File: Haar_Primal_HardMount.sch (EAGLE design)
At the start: 10 parts, among them J1 SOLDERCUP_CONN_QUAD, Q1 DMG3404, U1 SHT30DFN, U4 DPS368

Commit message: Updated Hard Mount - Variable address jumper
Added jumper to Hard Mount to allow for a variable address configuration
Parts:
- removed H2: (no value), bschulz:MOUNTING_HOLE2_NP
- added JP2: JUMPER-SMT_2_NO_SILK, bschulz:JUMPER-SMT_2_NO_SILK
- added R3: 10k, bschulz_passives:R-EU_10KR0603
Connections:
- new net ADDR: JP2.1, R3.2, U1.ADDR, U4.CSB
- net 3V3: now also JP2.2; no longer U4.CSB
- net GND: now also R3.1; no longer U1.ADDR
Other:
- moved on the sheet: C1, U4
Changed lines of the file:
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@@
 <setting verticaltext="up"/>
 </settings>
-<grid distance="0.1" unitdist="inch" unit="inch" style="lines" multiple="1" display="no" altdistance="0.01" altunitdist="inch" altunit="inch"/>
+<grid distance="0.1" unitdist="inch" unit="mm" style="lines" multiple="1" display="no" altdistance="0.01" altunitdist="inch" altunit="inch"/>
 <layers>
 <layer number="1" name="Top" color="4" fill="1" visible="no" active="no"/>
@@
 <part name="U1" library="bschulz" deviceset="SHT3*" device="DFN" technology="0" value="SHT30DFN"/>
 <part name="GND3" library="supply1" library_urn="urn:adsk.eagle:library:371" deviceset="GND" device=""/>
-<part name="H2" library="bschulz" deviceset="MOUNTING_HOLE" device="2_NP"/>
 <part name="JP1" library="bschulz" deviceset="JUMPER-SMT_3_2-NC_TRACE" device="_SILK" package3d_urn="urn:adsk.eagle:package:39289/1"/>
+<part name="R3" library="bschulz_passives" deviceset="R-EU_" device="R0603" technology="10K" value="10k"/>
+<part name="GND1" library="supply1" library_urn="urn:adsk.eagle:library:371" deviceset="GND" device=""/>
+<part name="JP2" library="bschulz" deviceset="JUMPER-SMT_2_NO" device="_SILK" package3d_urn="urn:adsk.eagle:package:39279/1"/>
 </parts>
 <sheets>
@@
 <attribute name="VALUE" x="41.402" y="62.23" size="1.778" layer="96" rot="R90"/>
 </instance>
-<instance part="U4" gate="G$1" x="93.98" y="27.94" smashed="yes">
-<attribute name="DISP" x="92.71" y="37.084" size="1.778" layer="95" align="center"/>
-<attribute name="NAME" x="92.71" y="21.59" size="1.27" layer="95" ratio="15" align="center"/>
-</instance>
-<instance part="C1" gate="G$1" x="68.58" y="30.48" smashed="yes">
-<attribute name="NAME" x="70.104" y="30.861" size="1.778" layer="95"/>
-<attribute name="VALUE" x="70.104" y="25.781" size="1.778" layer="96"/>
-</instance>
-<instance part="GND2" gate="1" x="76.2" y="20.32" smashed="yes">
-<attribute name="VALUE" x="73.66" y="17.78" size="1.778" layer="96"/>
+<instance part="U4" gate="G$1" x="93.98" y="55.88" smashed="yes">
+<attribute name="DISP" x="92.71" y="65.024" size="1.778" layer="95" align="center"/>
+<attribute name="NAME" x="92.71" y="49.53" size="1.27" layer="95" ratio="15" align="center"/>
+</instance>
+<instance part="C1" gate="G$1" x="58.42" y="58.42" smashed="yes">
+<attribute name="NAME" x="59.944" y="58.801" size="1.778" layer="95"/>
+<attribute name="VALUE" x="59.944" y="53.721" size="1.778" layer="96"/>
+</instance>
+<instance part="GND2" gate="1" x="76.2" y="48.26" smashed="yes">
+<attribute name="VALUE" x="73.66" y="45.72" size="1.778" layer="96"/>
 </instance>
 <instance part="U1" gate="G$1" x="33.02" y="27.94" smashed="yes">
@@
 <attribute name="VALUE" x="12.7" y="15.24" size="1.778" layer="96"/>
 </instance>
-<instance part="H2" gate="G$1" x="78.74" y="86.36" smashed="yes">
-<attribute name="NAME" x="80.772" y="86.9442" size="1.778" layer="95"/>
-<attribute name="VALUE" x="80.772" y="83.8962" size="1.778" layer="96"/>
-</instance>
 <instance part="JP1" gate="G$1" x="33.02" y="73.66" smashed="yes" rot="R270">
 <attribute name="NAME" x="33.401" y="71.12" size="1.778" layer="95" font="vector" rot="R270"/>
+</instance>
+<instance part="R3" gate="G$1" x="76.2" y="12.7" smashed="yes" rot="R90">
+<attribute name="NAME" x="74.7014" y="8.89" size="1.778" layer="95" rot="R90"/>
+<attribute name="VALUE" x="79.502" y="8.89" size="1.778" layer="96" rot="R90"/>
+</instance>
+<instance part="GND1" gate="1" x="76.2" y="2.54" smashed="yes">
+<attribute name="VALUE" x="73.66" y="0" size="1.778" layer="96"/>
+</instance>
+<instance part="JP2" gate="G$1" x="76.2" y="25.4" smashed="yes" rot="R90">
+<attribute name="NAME" x="73.66" y="22.86" size="1.778" layer="95" font="vector" rot="R90"/>
 </instance>
 </instances>
@@
 <segment>
 <pinref part="U4" gate="G$1" pin="GND"/>
-<wire x1="78.74" y1="25.4" x2="76.2" y2="25.4" width="0.1524" layer="91"/>
-<wire x1="76.2" y1="25.4" x2="76.2" y2="22.86" width="0.1524" layer="91"/>
+<wire x1="78.74" y1="53.34" x2="76.2" y2="53.34" width="0.1524" layer="91"/>
+<wire x1="76.2" y1="53.34" x2="76.2" y2="50.8" width="0.1524" layer="91"/>
 <pinref part="GND2" gate="1" pin="GND"/>
 <pinref part="C1" gate="G$1" pin="2"/>
-<wire x1="68.58" y1="25.4" x2="76.2" y2="25.4" width="0.1524" layer="91"/>
-<junction x="76.2" y="25.4"/>
-</segment>
-<segment>
-<pinref part="U1" gate="G$1" pin="ADDR"/>
+<wire x1="58.42" y1="53.34" x2="76.2" y2="53.34" width="0.1524" layer="91"/>
+<junction x="76.2" y="53.34"/>
+</segment>
+<segment>
 <pinref part="U1" gate="G$1" pin="VSS"/>
-<wire x1="17.78" y1="27.94" x2="17.78" y2="22.86" width="0.1524" layer="91"/>
 <wire x1="17.78" y1="22.86" x2="15.24" y2="22.86" width="0.1524" layer="91"/>
-<junction x="17.78" y="22.86"/>
 <wire x1="15.24" y1="22.86" x2="15.24" y2="20.32" width="0.1524" layer="91"/>
 <pinref part="GND3" gate="1" pin="GND"/>
+</segment>
+<segment>
+<pinref part="GND1" gate="1" pin="GND"/>
+<pinref part="R3" gate="G$1" pin="1"/>
+<wire x1="76.2" y1="5.08" x2="76.2" y2="7.62" width="0.1524" layer="91"/>
 </segment>
 </net>
@@
 <pinref part="U4" gate="G$1" pin="VDD"/>
 <pinref part="U4" gate="G$1" pin="VDDIO"/>
-<wire x1="78.74" y1="30.48" x2="78.74" y2="33.02" width="0.1524" layer="91"/>
-<junction x="78.74" y="33.02"/>
+<wire x1="78.74" y1="58.42" x2="78.74" y2="60.96" width="0.1524" layer="91"/>
+<junction x="78.74" y="60.96"/>
 <pinref part="C1" gate="G$1" pin="1"/>
-<wire x1="78.74" y1="33.02" x2="68.58" y2="33.02" width="0.1524" layer="91"/>
-<wire x1="68.58" y1="33.02" x2="63.5" y2="33.02" width="0.1524" layer="91"/>
-<junction x="68.58" y="33.02"/>
-<label x="63.5" y="33.02" size="0.8128" layer="95" rot="R180" xref="yes"/>
-<pinref part="U4" gate="G$1" pin="CSB"/>
-<wire x1="78.74" y1="30.48" x2="78.74" y2="27.94" width="0.1524" layer="91"/>
-<junction x="78.74" y="30.48"/>
+<wire x1="78.74" y1="60.96" x2="58.42" y2="60.96" width="0.1524" layer="91"/>
+<wire x1="58.42" y1="60.96" x2="53.34" y2="60.96" width="0.1524" layer="91"/>
+<junction x="58.42" y="60.96"/>
+<label x="53.34" y="60.96" size="0.8128" layer="95" rot="R180" xref="yes"/>
 </segment>
 <segment>
@@
 <label x="142.24" y="27.94" size="1.778" layer="95" rot="R180" xref="yes"/>
 </segment>
+<segment>
+<pinref part="JP2" gate="G$1" pin="2"/>
+<wire x1="76.2" y1="30.48" x2="76.2" y2="33.02" width="0.1524" layer="91"/>
+<wire x1="76.2" y1="33.02" x2="78.74" y2="33.02" width="0.1524" layer="91"/>
+<label x="78.74" y="33.02" size="1.27" layer="95" xref="yes"/>
+</segment>
 </net>
 <net name="SDA" class="0">
@@
 <segment>
 <pinref part="U4" gate="G$1" pin="SDI"/>
-<wire x1="106.68" y1="33.02" x2="114.3" y2="33.02" width="0.1524" layer="91"/>
-<label x="106.68" y="33.02" size="1.27" layer="95"/>
+<wire x1="106.68" y1="60.96" x2="114.3" y2="60.96" width="0.1524" layer="91"/>
+<label x="106.68" y="60.96" size="1.27" layer="95"/>
 </segment>
 <segment>
@@
 <segment>
 <pinref part="U4" gate="G$1" pin="SCK"/>
-<wire x1="106.68" y1="30.48" x2="114.3" y2="30.48" width="0.1524" layer="91"/>
-<label x="106.68" y="30.48" size="1.27" layer="95"/>
+<wire x1="106.68" y1="58.42" x2="114.3" y2="58.42" width="0.1524" layer="91"/>
+<label x="106.68" y="58.42" size="1.27" layer="95"/>
 </segment>
 <segment>
@@
 <segment>
 <pinref part="U4" gate="G$1" pin="SDO"/>
-<wire x1="106.68" y1="27.94" x2="114.3" y2="27.94" width="0.1524" layer="91"/>
-<label x="106.68" y="27.94" size="1.778" layer="95"/>
+<wire x1="106.68" y1="55.88" x2="114.3" y2="55.88" width="0.1524" layer="91"/>
+<label x="106.68" y="55.88" size="1.778" layer="95"/>
 </segment>
 </net>
@@
 </segment>
 </net>
+<net name="ADDR" class="0">
+<segment>
+<pinref part="U1" gate="G$1" pin="ADDR"/>
+<wire x1="17.78" y1="27.94" x2="15.24" y2="27.94" width="0.1524" layer="91"/>
+<label x="15.24" y="27.94" size="1.27" layer="95" rot="R180" xref="yes"/>
+</segment>
+<segment>
+<pinref part="U4" gate="G$1" pin="CSB"/>
+<wire x1="78.74" y1="55.88" x2="76.2" y2="55.88" width="0.1524" layer="91"/>
+<label x="76.2" y="55.88" size="1.27" layer="95" rot="R180" xref="yes"/>
+</segment>
+<segment>
+<pinref part="R3" gate="G$1" pin="2"/>
+<wire x1="76.2" y1="17.78" x2="76.2" y2="20.32" width="0.1524" layer="91"/>
+<wire x1="76.2" y1="20.32" x2="78.74" y2="20.32" width="0.1524" layer="91"/>
+<label x="78.74" y="20.32" size="1.27" layer="95" xref="yes"/>
+<pinref part="JP2" gate="G$1" pin="1"/>
+<junction x="76.2" y="20.32"/>
+</segment>
+</net>

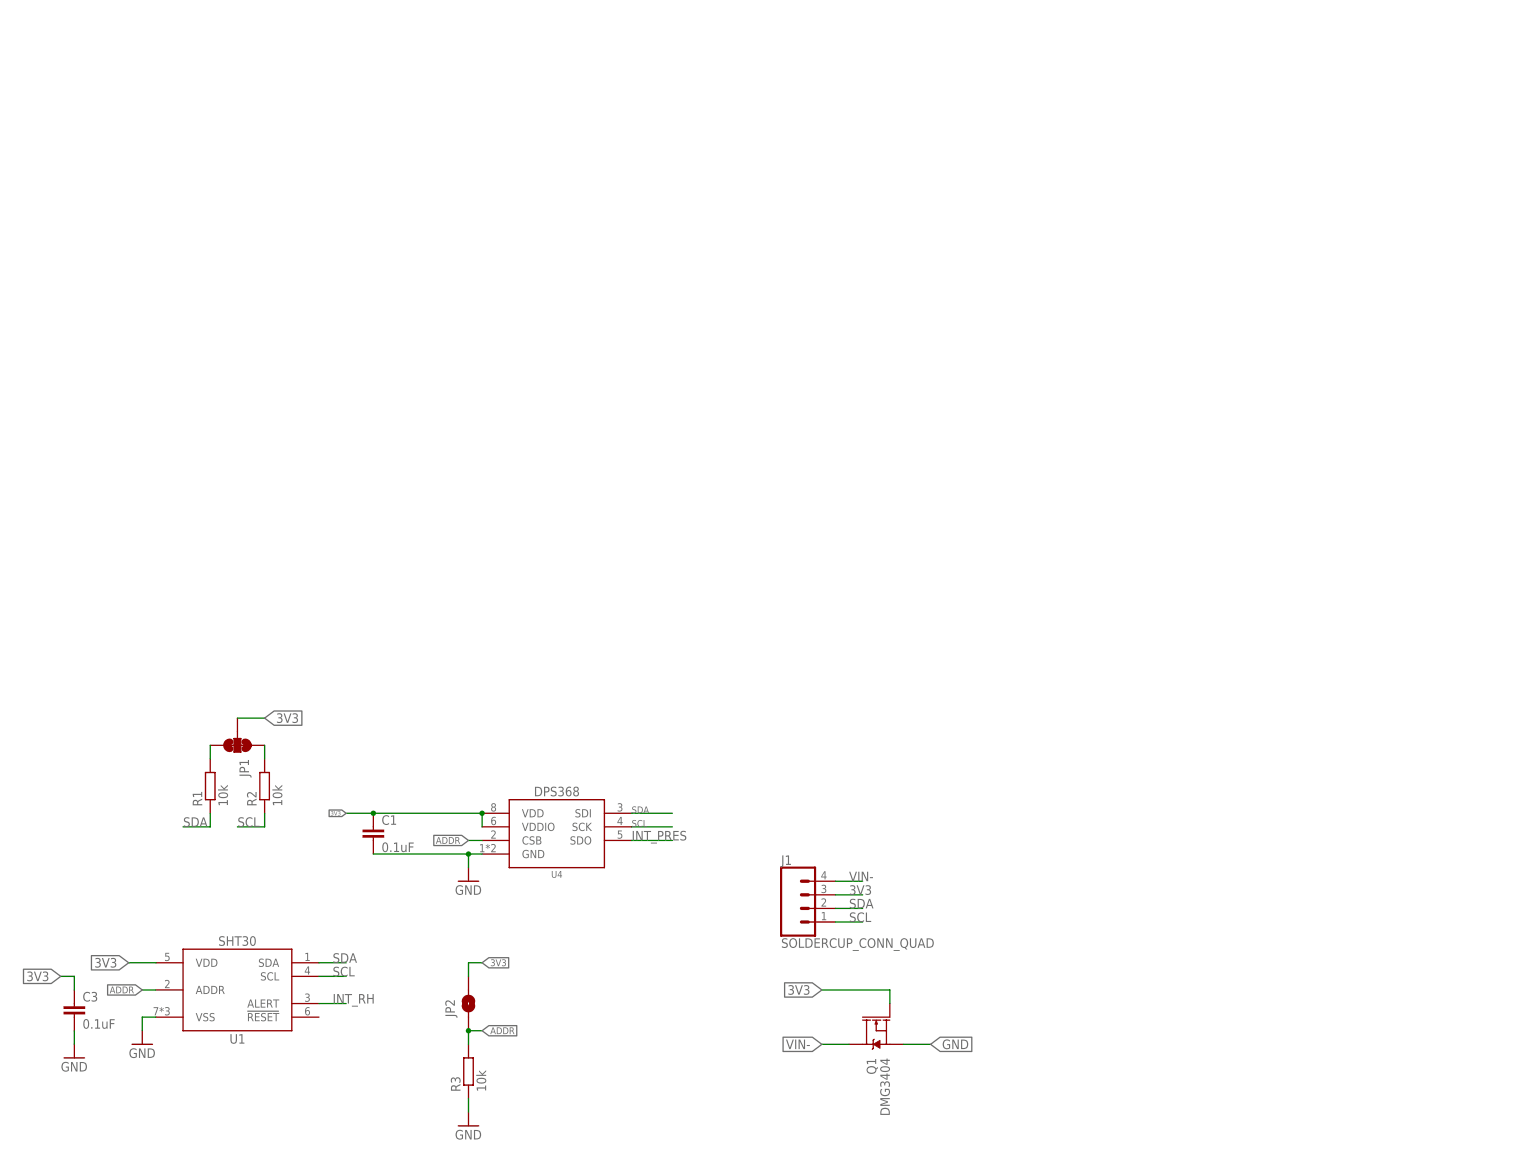
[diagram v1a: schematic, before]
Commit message: Hard Mount v1.1 Update
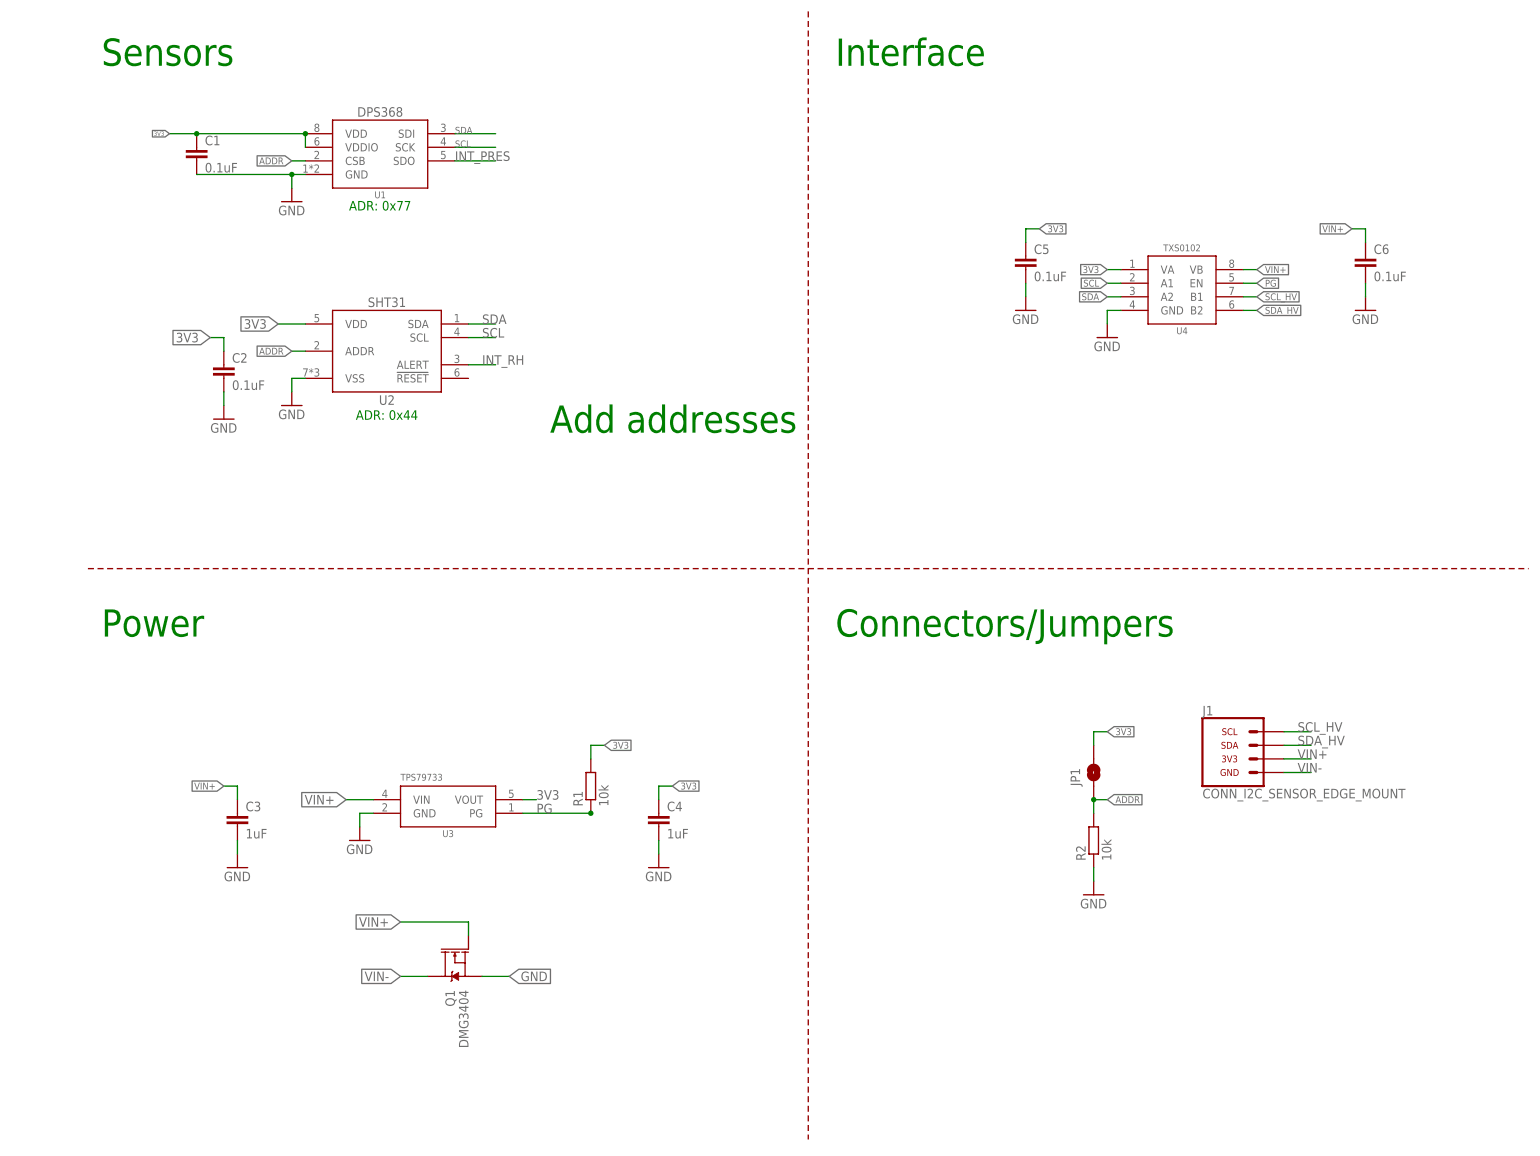
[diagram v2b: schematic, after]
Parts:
- removed JP2: JUMPER-SMT_2_NO_SILK, bschulz:JUMPER-SMT_2_NO_SILK
- removed R3: 10k, bschulz_passives:R-EU_10KR0603
- added C2, C5, C6: 0.1uF, bschulz_passives:C-EU0.1UFC0603
- added C4: 1uF, bschulz_passives:C-EU1UFC0603
- added U2: SHT31DFN, bschulz:SHT31DFN
- added U3: TPS79733, bschulz:TPS79733
- C3: value 0.1uF -> 1uF; device bschulz_passives:C-EU0.1UFC0603 -> bschulz_passives:C-EU1UFC0603
- J1: value SOLDERCUP_CONN_QUAD -> CONN_I2C_SENSOR_EDGE_MOUNT; device bschulz:SOLDERCUP_CONN_QUAD -> GEMS_Plugs:CONN_I2C_SENSOR_EDGE_MOUNT
- JP1: value JUMPER-SMT_3_2-NC_TRACE_SILK -> JUMPER-SMT_2_NO_SILK; device bschulz:JUMPER-SMT_3_2-NC_TRACE_SILK -> bschulz:JUMPER-SMT_2_NO_SILK
- U1: value SHT30DFN -> DPS368; device bschulz:SHT30DFN -> bschulz:DPS368
- U4: value DPS368 -> TXS0102DQM; device bschulz:DPS368 -> bschulz:TXS0102DQM
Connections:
- removed net N$1: JP1.3, R1.2
- removed net N$2: JP1.1, R2.2
- new net PG: R1.1, U3.PG, U4.EN
- new net SCL_HV: J1.SCL, U4.B1
- new net SDA_HV: J1.SDA, U4.B2
- new net VIN+: C3.1, C6.1, J1.3V3, Q1.G, U3.VIN, U4.VB
- net 3V3: now also C2.1, C4.1, C5.1, R1.2, U1.VDDIO, U2.VDD, U3.VOUT, U4.VA; no longer C3.1, J1.3, JP2.2, Q1.G, U4.VDD, U4.VDDIO
- net ADDR: now also JP1.1, R2.2, U1.CSB, U2.ADDR; no longer JP2.1, R3.2, U1.ADDR, U4.CSB
- net GND: now also C2.2, C4.2, C5.2, C6.2, R2.1, U1.GND, U2.VSS, U3.GND; no longer R3.1, U1.VSS
- net INT_PRES: now also U1.SDO; no longer U4.SDO
- net INT_RH: now also U2.ALERT; no longer U1.ALERT
- net SCL: now also U1.SCK, U2.SCL, U4.A1; no longer J1.1, R2.1, U1.SCL, U4.SCK
- net SDA: now also U1.SDI, U2.SDA, U4.A2; no longer J1.2, R1.1, U1.SDA, U4.SDI
- net VIN-: now also J1.GND; no longer J1.4
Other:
- note added: "ADR: 0x44"
- note added: "ADR: 0x77"
- note added: "Add addresses"
- note added: "Connectors/Jumpers"
- note added: "Interface"
- note added: "Power"
- note added: "Sensors"
- moved on the sheet: C1, C3, J1, Q1, R1, R2, U1

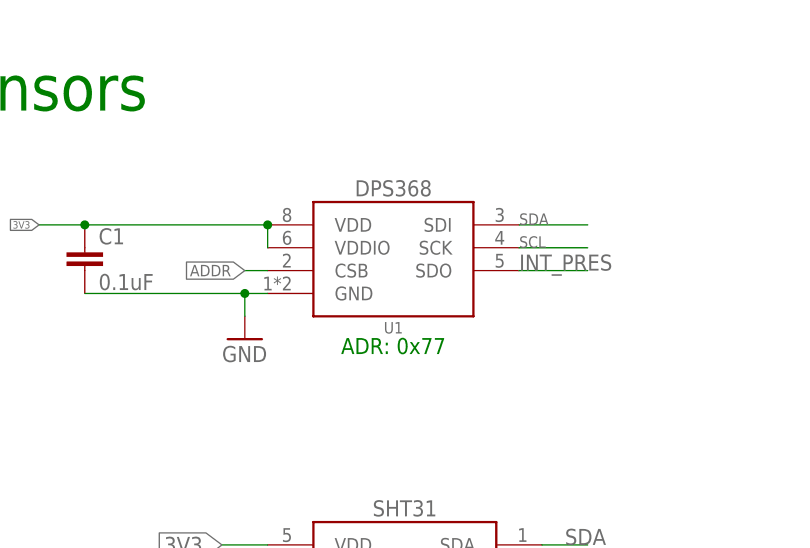
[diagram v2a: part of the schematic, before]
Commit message: v2.0 Updates - Generated Gerbers
Fixed ADDR pinout to DPS368
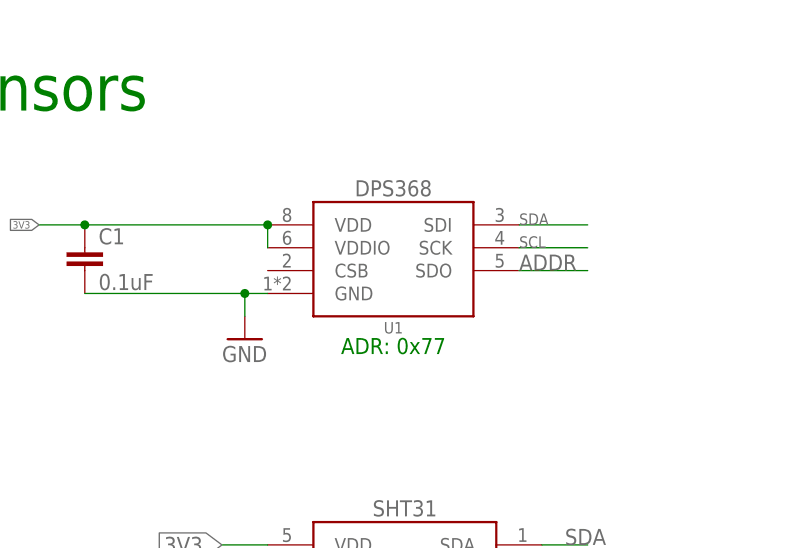
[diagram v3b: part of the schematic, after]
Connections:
- removed net INT_PRES: U1.SDO
- net ADDR: now also U1.SDO; no longer U1.CSB
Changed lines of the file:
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@@
 <attribute name="DESIGNER" value="Bobby Schulz"/>
 <attribute name="PROJECT" value="Haar-Primal"/>
-<attribute name="REV" value="v0.1"/>
+<attribute name="REV" value="v2.0"/>
 </part>
 <part name="J1" library="GEMS_Plugs" deviceset="CONN_I2C_SENSOR" device="_EDGE_MOUNT"/>
@@
 </segment>
 </net>
-<net name="INT_PRES" class="0">
-<segment>
-<pinref part="U1" gate="G$1" pin="SDO"/>
-<wire x1="73.66" y1="182.88" x2="81.28" y2="182.88" width="0.1524" layer="91"/>
-<label x="73.66" y="182.88" size="1.778" layer="95"/>
-</segment>
-</net>
 <net name="INT_RH" class="0">
 <segment>
@@
 <wire x1="45.72" y1="147.32" x2="43.18" y2="147.32" width="0.1524" layer="91"/>
 <label x="43.18" y="147.32" size="1.27" layer="95" rot="R180" xref="yes"/>
-</segment>
-<segment>
-<pinref part="U1" gate="G$1" pin="CSB"/>
-<wire x1="45.72" y1="182.88" x2="43.18" y2="182.88" width="0.1524" layer="91"/>
-<label x="43.18" y="182.88" size="1.27" layer="95" rot="R180" xref="yes"/>
 </segment>
 <segment>
@@
 <junction x="193.04" y="63.5"/>
 </segment>
-</net>
+<segment>
+<pinref part="U1" gate="G$1" pin="SDO"/>
+<wire x1="73.66" y1="182.88" x2="81.28" y2="182.88" width="0.1524" layer="91"/>
+<label x="73.66" y="182.88" size="1.778" layer="95"/>
+</segment>
+</net>
